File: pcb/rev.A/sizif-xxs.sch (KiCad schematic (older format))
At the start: 95 parts, among them J1 Pin header 1x2 Pitch=2.54mm, J2 USB_B_Micro, J3 PJ-320D, J4 PJ-320D, J5 Pin header 1x4 Pitch=2.54mm, J6 Solder points, J7 DM3D-SF, Q1 BC817, Q2 BSS138, Q3 BSS138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

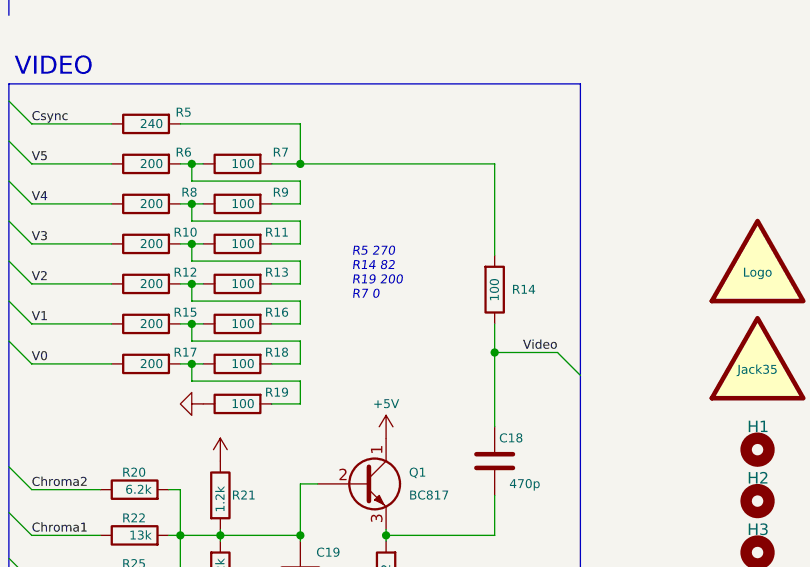
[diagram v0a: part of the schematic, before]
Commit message: replace composite video output implementation
New one is borrowed from Speccy 2010 project. It's have a much, much
better output quality in price of increased FPGA resources usage.
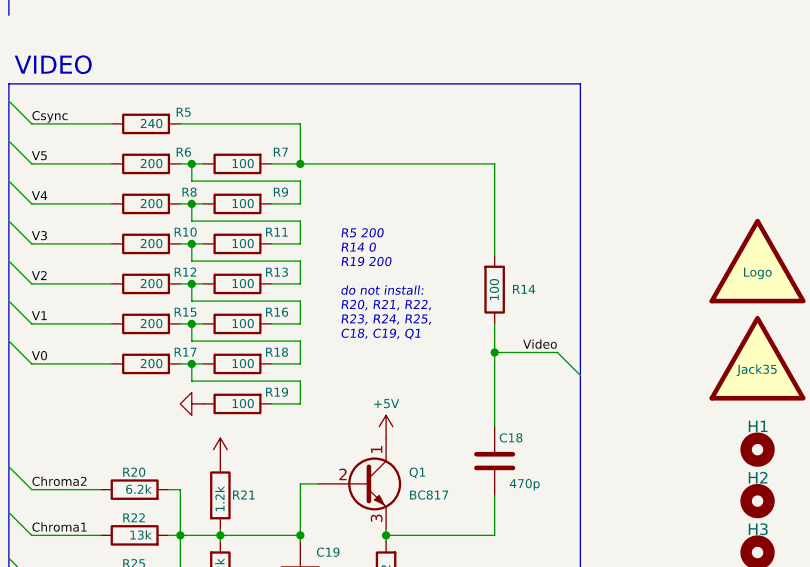
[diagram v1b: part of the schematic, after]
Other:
- note added: "R5 200\nR14 0\nR19 200\n\ndo not install:\nR20, R21, R22,\nR23, R24, R25,\nC18, C19, Q1"
- note removed: "R5 270\nR14 82\nR19 200\nR7 0"
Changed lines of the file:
@@
 	11375 2050 11725 2050
 NoConn ~ 11175 6475
-Text Notes 9700 3775 0    39   Italic 0
-R5 270\nR14 82\nR19 200\nR7 0
 Wire Bus Line
 	4925 675  3225 675
@@
 Wire Bus Line
 	625  675  625  4025
+Text Notes 9650 3950 0    39   Italic 0
+R5 200\nR14 0\nR19 200\n\ndo not install:\nR20, R21, R22,\nR23, R24, R25,\nC18, C19, Q1
 $EndSCHEMATC
